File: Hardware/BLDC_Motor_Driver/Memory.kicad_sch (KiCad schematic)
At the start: 8 parts, among them U3 25LC256-E_SN

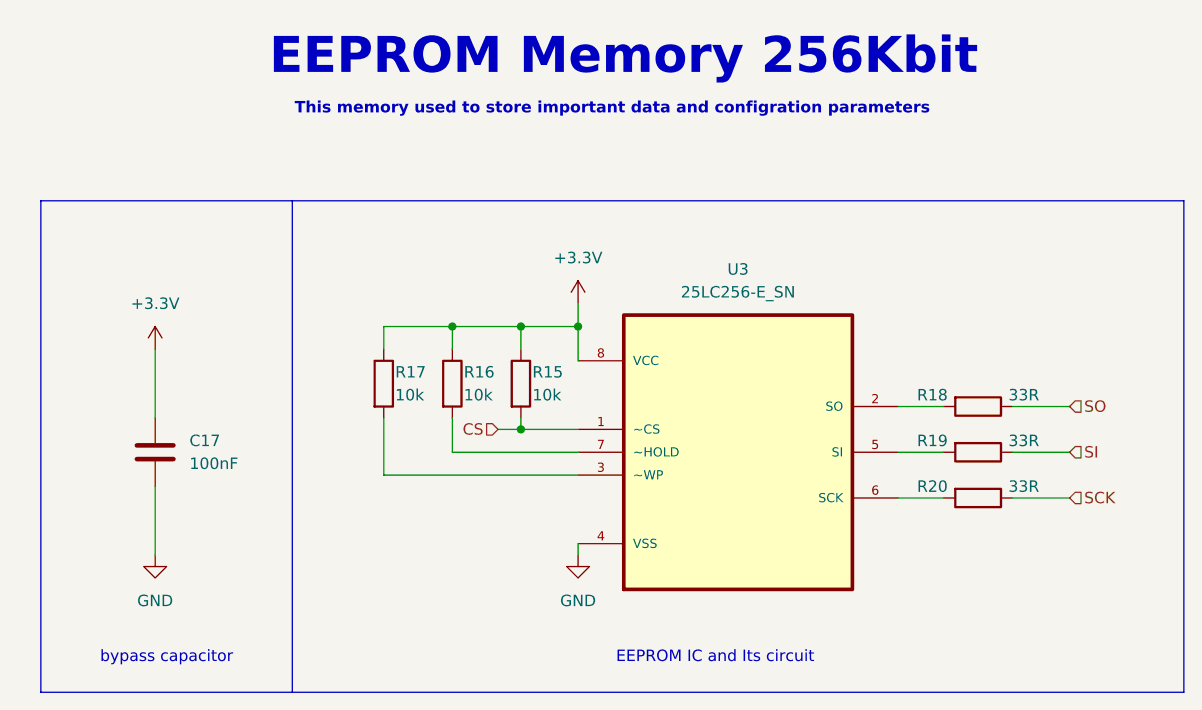
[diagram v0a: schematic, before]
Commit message: add CS series resistor to EEPROM Schematic
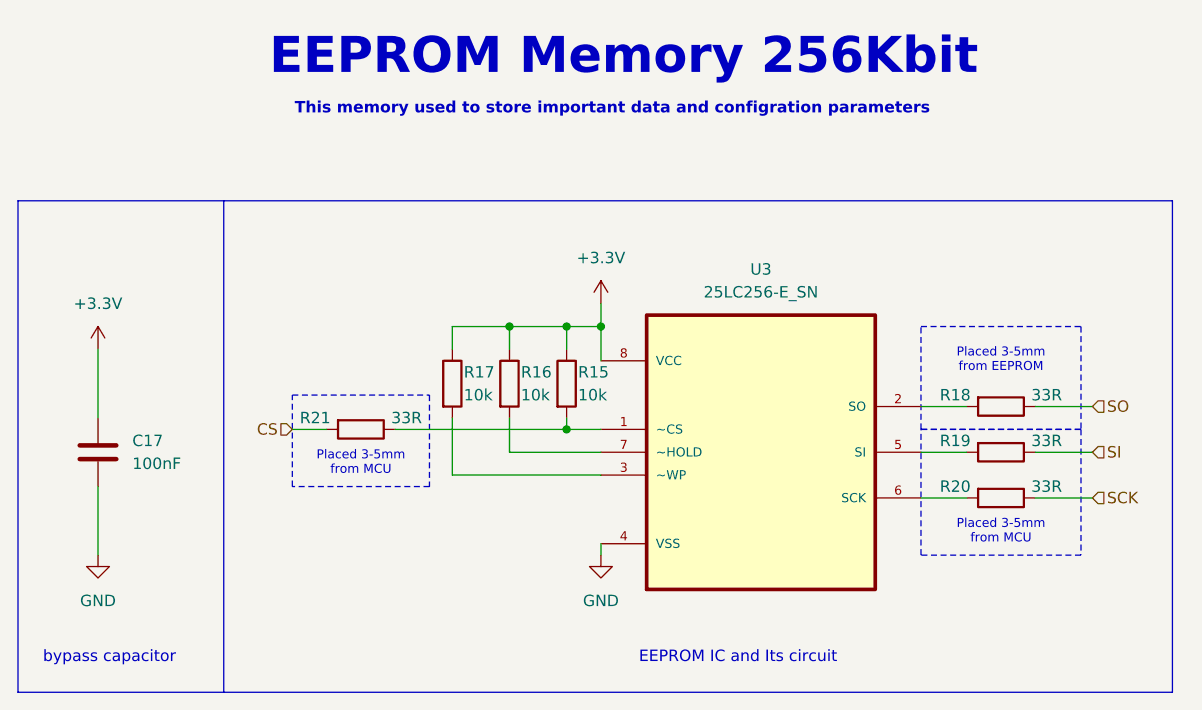
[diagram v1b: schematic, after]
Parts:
- added R21: 33R, Resistor_SMD:R_0603_1608Metric, symbol Device:R
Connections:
- net CS: now also R21.2; no longer R15.2, U3.1 (~CS)
- new net: R15.2, R21.1, U3.1 (~CS)
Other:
- note added: "Placed 3-5mm from EEPROM"
- note added: "Placed 3-5mm from MCU"
- moved on the sheet: C17, R15, R16, R17, R18, R19, R20, U3
